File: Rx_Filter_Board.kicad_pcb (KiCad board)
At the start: 2 copper layers, 100 parts, among them K1 HK4100, K10 HK4100, K11 HK4100, K12 HK4100, K13 HK4100, K2 HK4100, K3 HK4100, K4 HK4100, K5 HK4100, K6 HK4100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

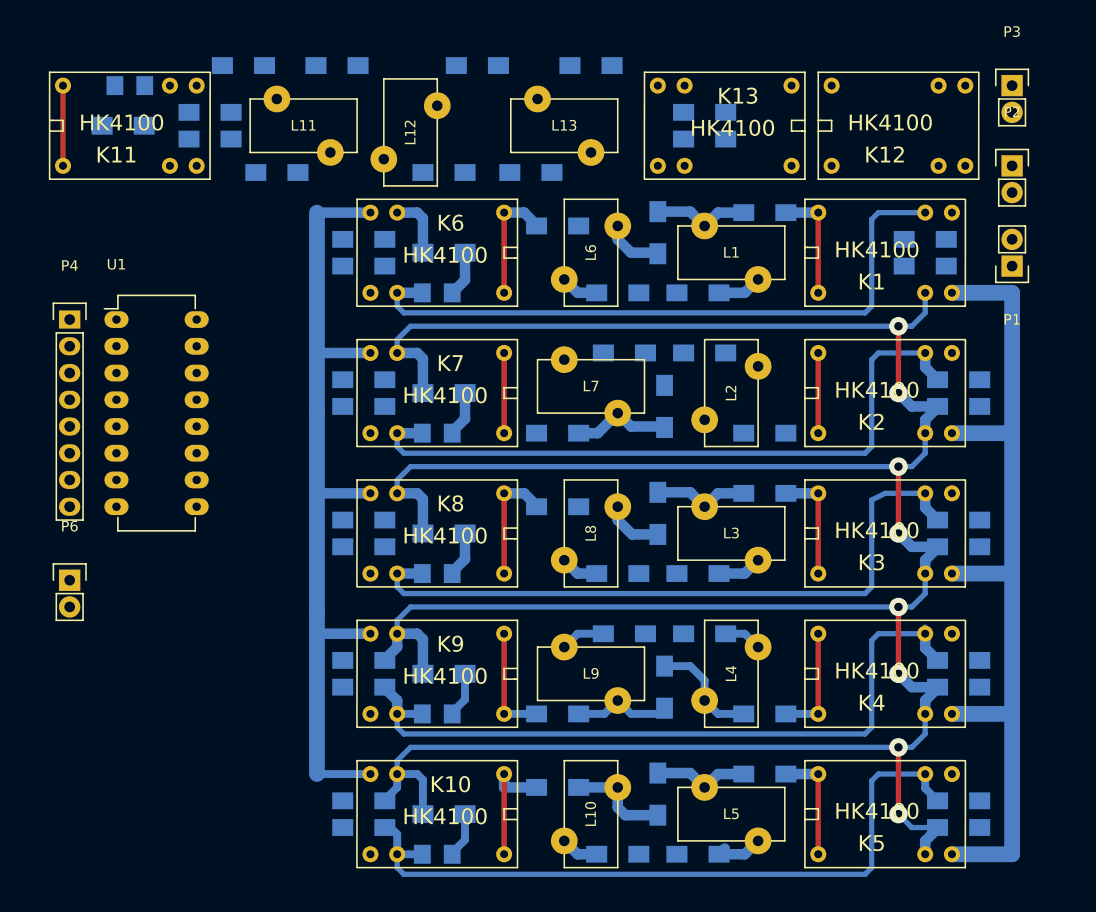
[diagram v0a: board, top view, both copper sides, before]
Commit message: Setting up ground plane
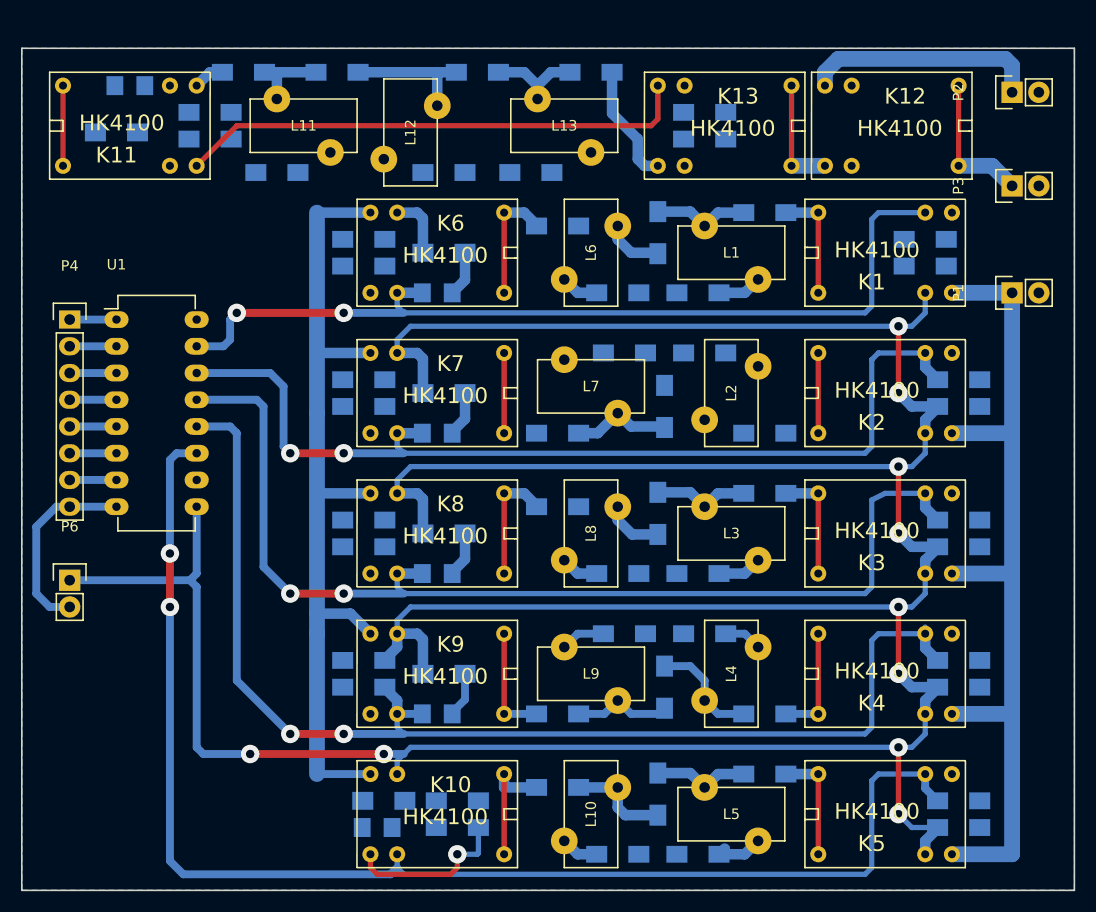
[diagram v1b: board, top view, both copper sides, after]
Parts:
- moved P3 9.52 mm to (132.1, 52.1), turned to 90 degrees
- moved C46 8.89 mm to (79.4, 113.0), turned to 0 degrees
- moved C51 8.89 mm to (79.4, 110.5), turned to 0 degrees
- moved P2 6.98 mm to (132.1, 43.2), turned to 90 degrees
- moved D5 6.25 mm to (71.8, 113.0), turned to 180 degrees
- moved R5 5.85 mm to (72.4, 110.5), turned to 180 degrees
- moved P1 2.54 mm to (132.1, 62.2), turned to 90 degrees
- moved R6 0.90 mm to (47.0, 47.0)
- moved C26 0.63 mm to (59.1, 41.3)
- moved C28 0.63 mm to (67.9, 41.3)
- moved C30 0.63 mm to (81.3, 41.3)
- moved C32 0.63 mm to (92.1, 41.3)
- moved K12 0.63 mm to (120.7, 46.4), turned to 0 degrees
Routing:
- net Net-(C41-Pad1): track 69.3 -> 126.9 mm, vias 0 -> 2
- net Net-(K11-Pad6): track 0.00 -> 48.8 mm
- net +12v: track 307.9 -> 353.7 mm, vias 8 -> 10
- net Net-(C40-Pad1): track 69.6 -> 115.1 mm, vias 0 -> 2
- net Net-(C39-Pad1): track 65.8 -> 102.0 mm, vias 0 -> 2
- net GND: track 0.00 -> 34.9 mm, vias 0 -> 1
- net Net-(C38-Pad1): track 65.9 -> 92.1 mm, vias 0 -> 2
- net Net-(K12-Pad6): track 0.00 -> 22.4 mm
- net Net-(C37-Pad1): track 62.9 -> 85.0 mm, vias 0 -> 2
- net Net-(K12-Pad3): track 0.00 -> 13.5 mm
- net Net-(C28-Pad1): track 0.00 -> 12.5 mm
- net Net-(C32-Pad1): track 0.00 -> 11.4 mm
- net Net-(K12-Pad1): track 0.00 -> 10.8 mm
- net Net-(C30-Pad1): track 0.00 -> 10.4 mm
- net Net-(C26-Pad1): track 0.00 -> 7.43 mm
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- added copper zone on B.Cu, net GND
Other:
- board outline added: 100 x 80 mm

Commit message: A usable board at this point
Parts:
- moved C11 0.63 mm to (98.4, 57.1)
- moved C29 0.63 mm to (78.1, 50.2)
- moved C31 0.63 mm to (86.4, 50.2)
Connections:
- K1 pad 4: Net-(C1-Pad2) -> (no net)
- K10 pad 3: Net-(C25-Pad1) -> (no net)
- K2 pad 3: Net-(C2-Pad2) -> (no net)
- K3 pad 4: Net-(C3-Pad2) -> (no net)
- K4 pad 3: Net-(C4-Pad2) -> (no net)
- K5 pad 4: Net-(C5-Pad2) -> (no net)
- K6 pad 3: Net-(C21-Pad1) -> (no net)
- K7 pad 4: Net-(C22-Pad1) -> (no net)
- K8 pad 3: Net-(C23-Pad1) -> (no net)
- K9 pad 4: Net-(C24-Pad1) -> (no net)
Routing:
- net GND: track 34.9 -> 360.9 mm, vias 1 -> 20
- net +12v: track 353.7 -> 589.5 mm
- net Net-(K12-Pad2): track 0.00 -> 91.7 mm, vias 0 -> 3
- net Net-(C52-Pad1): track 0.00 -> 86.0 mm, vias 0 -> 3
- net Net-(K10-Pad6): track 87.1 -> 121.6 mm
- net Net-(K1-Pad6): track 81.9 -> 100.8 mm
- net Net-(C12-Pad2): track 0.00 -> 10.5 mm
- net Net-(C41-Pad1): track 126.9 -> 136.0 mm, vias 2 -> 4
- net Net-(C4-Pad2): track 10.7 -> 3.08 mm
- net Net-(C3-Pad2): track 10.7 -> 3.08 mm
- net Net-(C24-Pad1): track 10.7 -> 3.08 mm
- net Net-(C23-Pad1): track 11.3 -> 3.66 mm
- net Net-(C21-Pad1): track 11.3 -> 3.66 mm
- net Net-(C1-Pad2): track 10.7 -> 3.08 mm
- net Net-(C5-Pad2): track 10.7 -> 3.08 mm
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
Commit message: Saving home brew lazer board layout in branch Hbrew
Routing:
- net Net-(K1-Pad6): track 100.8 -> 96.9 mm
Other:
- board text added: "ZL2APV"
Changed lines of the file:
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@@
   (general
     (links 196)
-    (no_connects 0)
-    (area 37.511667 38 138.075001 119.075001)
+    (no_connects 1)
+    (area 37.924999 38.924999 138.075001 119.075001)
     (thickness 1.6)
-    (drawings 4)
-    (tracks 544)
+    (drawings 11)
+    (tracks 545)
     (zones 0)
     (modules 100)
@@
   )
   (setup
-    (last_trace_width 0.75)
+    (last_trace_width 0.25)
     (user_trace_width 0.5)
     (user_trace_width 0.75)
@@
     (user_via 1.5 0.8)
     (user_via 1.75 0.8)
+    (user_via 3.4 3.3)
     (uvia_size 0.3)
     (uvia_drill 0.1)
@@
     (visible_elements 7FFFFFFF)
     (pcbplotparams
-      (layerselection 0x00030_80000001)
+      (layerselection 0x01000_80000000)
       (usegerberextensions false)
-      (excludeedgelayer true)
+      (excludeedgelayer false)
       (linewidth 0.100000)
       (plotframeref false)
@@
       (psnegative false)
       (psa4output false)
-      (plotreference true)
-      (plotvalue true)
+      (plotreference false)
+      (plotvalue false)
       (plotinvisibletext false)
       (padsonsilk false)
       (subtractmaskfromsilk false)
-      (outputformat 1)
-      (mirror false)
+      (outputformat 2)
+      (mirror true)
       (drillshape 1)
       (scaleselection 1)
@@
     )
   )
+  (gr_text ZL2APV (at 57.785 94.615 90) (layer B.Cu)
+    (effects (font (size 2.2 2.2) (thickness 0.4)))
+  )
+  (dimension 80 (width 0.3) (layer Dwgs.User)
+    (gr_text "80.000 mm" (at 146 79 270) (layer Dwgs.User)
+      (effects (font (size 1.5 1.5) (thickness 0.3)))
+    )
+    (feature1 (pts (xy 144 119) (xy 144 119)))
+    (feature2 (pts (xy 144 39) (xy 144 39)))
+    (crossbar (pts (xy 144 39) (xy 144 119)))
+    (arrow1a (pts (xy 144 119) (xy 143.413579 117.873496)))
+    (arrow1b (pts (xy 144 119) (xy 144.586421 117.873496)))
+    (arrow2a (pts (xy 144 39) (xy 143.413579 40.126504)))
+    (arrow2b (pts (xy 144 39) (xy 144.586421 40.126504)))
+  )
+  (gr_line (start 139 119) (end 145 119) (angle 90) (layer Dwgs.User) (width 0.2))
+  (gr_line (start 139 39) (end 145 39) (angle 90) (layer Dwgs.User) (width 0.2))
+  (dimension 100 (width 0.3) (layer Dwgs.User)
+    (gr_text "100.000 mm" (at 88 32) (layer Dwgs.User)
+      (effects (font (size 1.5 1.5) (thickness 0.3)))
+    )
+    (feature1 (pts (xy 138 34) (xy 138 36.7)))
+    (feature2 (pts (xy 38 34) (xy 38 36.7)))
+    (crossbar (pts (xy 38 34) (xy 138 34)))
+    (arrow1a (pts (xy 138 34) (xy 136.873496 34.586421)))
+    (arrow1b (pts (xy 138 34) (xy 136.873496 33.413579)))
+    (arrow2a (pts (xy 38 34) (xy 39.126504 34.586421)))
+    (arrow2b (pts (xy 38 34) (xy 39.126504 33.413579)))
+  )
+  (gr_line (start 138 38) (end 138 32) (angle 90) (layer Dwgs.User) (width 0.2))
+  (gr_line (start 38 38) (end 38 32) (angle 90) (layer Dwgs.User) (width 0.2))
   (gr_line (start 38 39) (end 38 119) (angle 90) (layer Edge.Cuts) (width 0.15))
   (gr_line (start 138 39) (end 38 39) (angle 90) (layer Edge.Cuts) (width 0.15))
@@
   (segment (start 46.355 42.545) (end 44.99 43.91) (width 1) (layer B.Cu) (net 45))
   (segment (start 44.99 43.91) (end 44.99 46.99) (width 1) (layer B.Cu) (net 45))
+  (segment (start 134 102.235) (end 134 112) (width 0.5) (layer F.Cu) (net 46))
+  (segment (start 130.43 115.57) (end 126.365 115.57) (width 0.5) (layer F.Cu) (net 46))
+  (segment (start 134 112) (end 130.43 115.57) (width 0.25) (layer F.Cu) (net 46))
   (segment (start 126.365 75.565) (end 136.525 75.565) (width 0.75) (layer F.Cu) (net 46))
   (segment (start 126.365 88.9) (end 136.525 88.9) (width 0.75) (layer F.Cu) (net 46))
-  (segment (start 126.365 102.235) (end 136.525 102.235) (width 0.75) (layer F.Cu) (net 46))
+  (segment (start 126.365 102.235) (end 134 102.235) (width 0.75) (layer F.Cu) (net 46))
+  (segment (start 134 102.235) (end 136.525 102.235) (width 0.75) (layer F.Cu) (net 46))
   (segment (start 132.08 62.23) (end 132.08 64.77) (width 0.75) (layer F.Cu) (net 46))
-  (segment (start 135.255 115.57) (end 126.365 115.57) (width 0.75) (layer F.Cu) (net 46))
-  (segment (start 136.525 114.3) (end 135.255 115.57) (width 0.75) (layer F.Cu) (net 46))
   (segment (start 136.525 69.215) (end 136.525 75.565) (width 0.75) (layer F.Cu) (net 46))
   (segment (start 136.525 75.565) (end 136.525 88.9) (width 0.75) (layer F.Cu) (net 46))
   (segment (start 136.525 88.9) (end 136.525 102.235) (width 0.75) (layer F.Cu) (net 46))
-  (segment (start 136.525 102.235) (end 136.525 114.3) (width 0.75) (layer F.Cu) (net 46))
   (segment (start 132.08 64.77) (end 136.525 69.215) (width 0.75) (layer F.Cu) (net 46))
   (segment (start 126.365 62.23) (end 132.08 62.23) (width 1.5) (layer B.Cu) (net 46))
@@
   (segment (start 100.87 50.07) (end 100.965 50.165) (width 0.75) (layer B.Cu) (net 66))
   (zone (net 12) (net_name GND) (layer B.Cu) (hatch edge 0.508)
-    (connect_pads yes (clearance 1))
+    (connect_pads (clearance 1))
     (min_thickness 0.508)
-    (fill yes (arc_segments 16) (thermal_gap 0.508) (thermal_bridge_width 0.5))
+    (fill yes (arc_segments 16) (thermal_gap 0.508) (thermal_bridge_width 1))
     (polygon
       (pts

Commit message: Filter progress
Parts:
- added CNR1: 1pin, Connect:1pin, F.Cu at (94.0, 66.0)
- added CNR2: 1pin, Connect:1pin, F.Cu at (94.0, 134.0)
- added CNR3: 1pin, Connect:1pin, F.Cu at (182.0, 134.0)
- added CVR4: 1pin, Connect:1pin, F.Cu at (182.0, 66.0)
- moved P2 71.6 mm to (196.8, 73.7)
- moved P3 71.1 mm to (196.8, 81.3)
- moved P1 69.8 mm to (196.8, 88.3)
- moved R6 65.6 mm to (106.7, 74.3), turned to 270 degrees
- moved K11 64.5 mm to (106.7, 73.7), turned to 270 degrees
- moved D6 64.0 mm to (103.5, 74.9), turned to 270 degrees
- moved C53 60.2 mm to (109.9, 74.3), turned to 270 degrees
- moved C28 59.1 mm to (121.9, 65.4)
- moved L11 58.3 mm to (123.2, 67.3)
- moved L12 58.3 mm to (130.8, 75.6)
- moved C27 58.3 mm to (115.6, 74.3)
- moved C30 57.4 mm to (133.3, 65.4)
- moved C29 57.1 mm to (130.2, 73.7)
- moved C32 56.8 mm to (143.5, 65.4)
- moved C1 56.2 mm to (158.8, 80.0)
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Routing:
- net GND: track 360.9 -> 30.7 mm, vias 20 -> 0
- net +12v: track 589.5 -> 419.1 mm, vias 10 -> 0
- net Net-(K10-Pad6): track 121.6 -> 0.00 mm
- net Net-(K1-Pad6): track 96.9 -> 0.00 mm
- net Net-(K12-Pad2): track 91.7 -> 0.00 mm, vias 3 -> 0
- net Net-(C41-Pad1): track 136.0 -> 69.7 mm, vias 4 -> 1
- net Net-(K11-Pad6): track 49.7 -> 0.00 mm
- net Net-(C52-Pad1): track 86.0 -> 39.5 mm, vias 3 -> 0
- net Net-(C40-Pad1): track 115.4 -> 70.3 mm, vias 0 -> 2
- net Net-(C39-Pad1): track 104.7 -> 69.8 mm, vias 0 -> 2
- net Net-(C38-Pad1): track 95.1 -> 69.7 mm, vias 0 -> 2
- net Net-(C37-Pad1): track 90.3 -> 67.0 mm, vias 0 -> 2
- net Net-(K12-Pad6): track 22.4 -> 0.00 mm
- net Net-(C28-Pad1): track 12.5 -> 0.00 mm
- net Net-(C30-Pad1): track 10.4 -> 0.00 mm
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- removed copper zone on B.Cu, net GND
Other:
- board size 100 x 80 mm -> 100 x 100 mm

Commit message: Layout completed
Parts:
- moved P2 34.3 mm to (164.5, 62.2)
- moved P3 15.4 mm to (183.5, 73.7), turned to 0 degrees
- moved P1 13.4 mm to (183.5, 89.5), turned to 0 degrees
- moved C46 8.89 mm to (120.7, 133.3), turned to 180 degrees
- moved C51 8.89 mm to (120.7, 130.8), turned to 180 degrees
- moved D5 6.25 mm to (127.6, 135.9), turned to 0 degrees
- moved R5 5.85 mm to (128.3, 132.1), turned to 0 degrees
- moved C32 2.54 mm to (143.5, 67.9)
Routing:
- net GND: track 30.7 -> 491.7 mm, vias 0 -> 116
- net +12v: track 419.1 -> 519.8 mm, vias 0 -> 4
- net Net-(K12-Pad2): track 0.00 -> 94.9 mm, vias 0 -> 2
- net Net-(K10-Pad6): track 0.00 -> 73.6 mm
- net Net-(K1-Pad6): track 0.00 -> 60.1 mm
- net Net-(C41-Pad1): track 69.7 -> 127.4 mm, vias 1 -> 2
- net Net-(C52-Pad1): track 39.5 -> 92.7 mm
- net Net-(C40-Pad1): track 70.3 -> 118.2 mm, vias 2 -> 3
- net Net-(K11-Pad6): track 0.00 -> 43.7 mm
- net Net-(C39-Pad1): track 69.8 -> 109.6 mm, vias 2 -> 3
- net Net-(C38-Pad1): track 69.7 -> 98.6 mm, vias 2 -> 3
- net Net-(C37-Pad1): track 67.0 -> 90.5 mm, vias 2 -> 3
- net Net-(C28-Pad1): track 0.00 -> 10.2 mm, vias 0 -> 2
- net Net-(C30-Pad1): track 0.00 -> 7.21 mm
- net Net-(K12-Pad3): track 7.62 -> 14.0 mm
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- added copper zone on B.Cu, net GND
- added copper zone on F.Cu, net GND

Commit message: Final fabrication with LCD serial driver added
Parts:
- added DS1: LCD16X2, Pin_Headers:Pin_Header_Straight_1x14, F.Cu at (183.8, 157.9)
- added DS1: LCD16X2, Pin_Headers:Pin_Header_Straight_1x14, F.Cu at (126.6, 157.9)
- added Da1: 1N914, Diodes_ThroughHole:Diode_DO-35_SOD27_Horizontal_RM10, F.Cu at (160.9, 154.7)
- added Da1: 1N914, Diodes_ThroughHole:Diode_DO-35_SOD27_Horizontal_RM10, F.Cu at (103.8, 154.7)
- added Pa1: CONN_01X05, Pin_Headers:Pin_Header_Straight_1x05, F.Cu at (173.6, 143.3)
- added Pa1: CONN_01X05, Pin_Headers:Pin_Header_Straight_1x05, F.Cu at (116.5, 143.3)
- added Ra1: 1k, Resistors_SMD:R_1206_HandSoldering, B.Cu at (176.1, 150.9)
- added Ra1: 1k, Resistors_SMD:R_1206_HandSoldering, B.Cu at (119.0, 150.9)
- added Ua1: 74LS164, Housings_DIP:DIP-14_W7.62mm_LongPads, F.Cu at (152.0, 150.9)
- added Ua1: 74LS164, Housings_DIP:DIP-14_W7.62mm_LongPads, F.Cu at (94.9, 150.9)
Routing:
- net Net-(DS1-Pad2): track 0.00 -> 101.0 mm
- net Net-(Pa1-Pad2): track 0.00 -> 65.1 mm, vias 0 -> 2
- net Net-(DS1-Pad1): track 0.00 -> 62.2 mm, vias 0 -> 2
- net Net-(DS1-Pad12): track 0.00 -> 59.0 mm
- net Net-(DS1-Pad13): track 0.00 -> 52.8 mm
- net Net-(Da1-Pad1): track 0.00 -> 50.4 mm
- net Net-(DS1-Pad14): track 0.00 -> 46.5 mm
- net Net-(DS1-Pad4): track 0.00 -> 37.3 mm, vias 0 -> 2
- net Net-(DS1-Pad3): track 0.00 -> 29.2 mm
- net Net-(DS1-Pad11): track 0.00 -> 25.2 mm
- net Net-(DS1-Pad6): track 0.00 -> 19.6 mm
- net Net-(Pa1-Pad1): track 0.00 -> 12.7 mm
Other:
- board text added: "Rx Filter by ZL2APV 2016/10/11"
- board text removed: "ZL2APV"
